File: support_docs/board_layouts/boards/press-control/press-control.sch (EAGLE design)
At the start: 14 parts, among them X3 6ESRM-P, X4 6ESRM-P

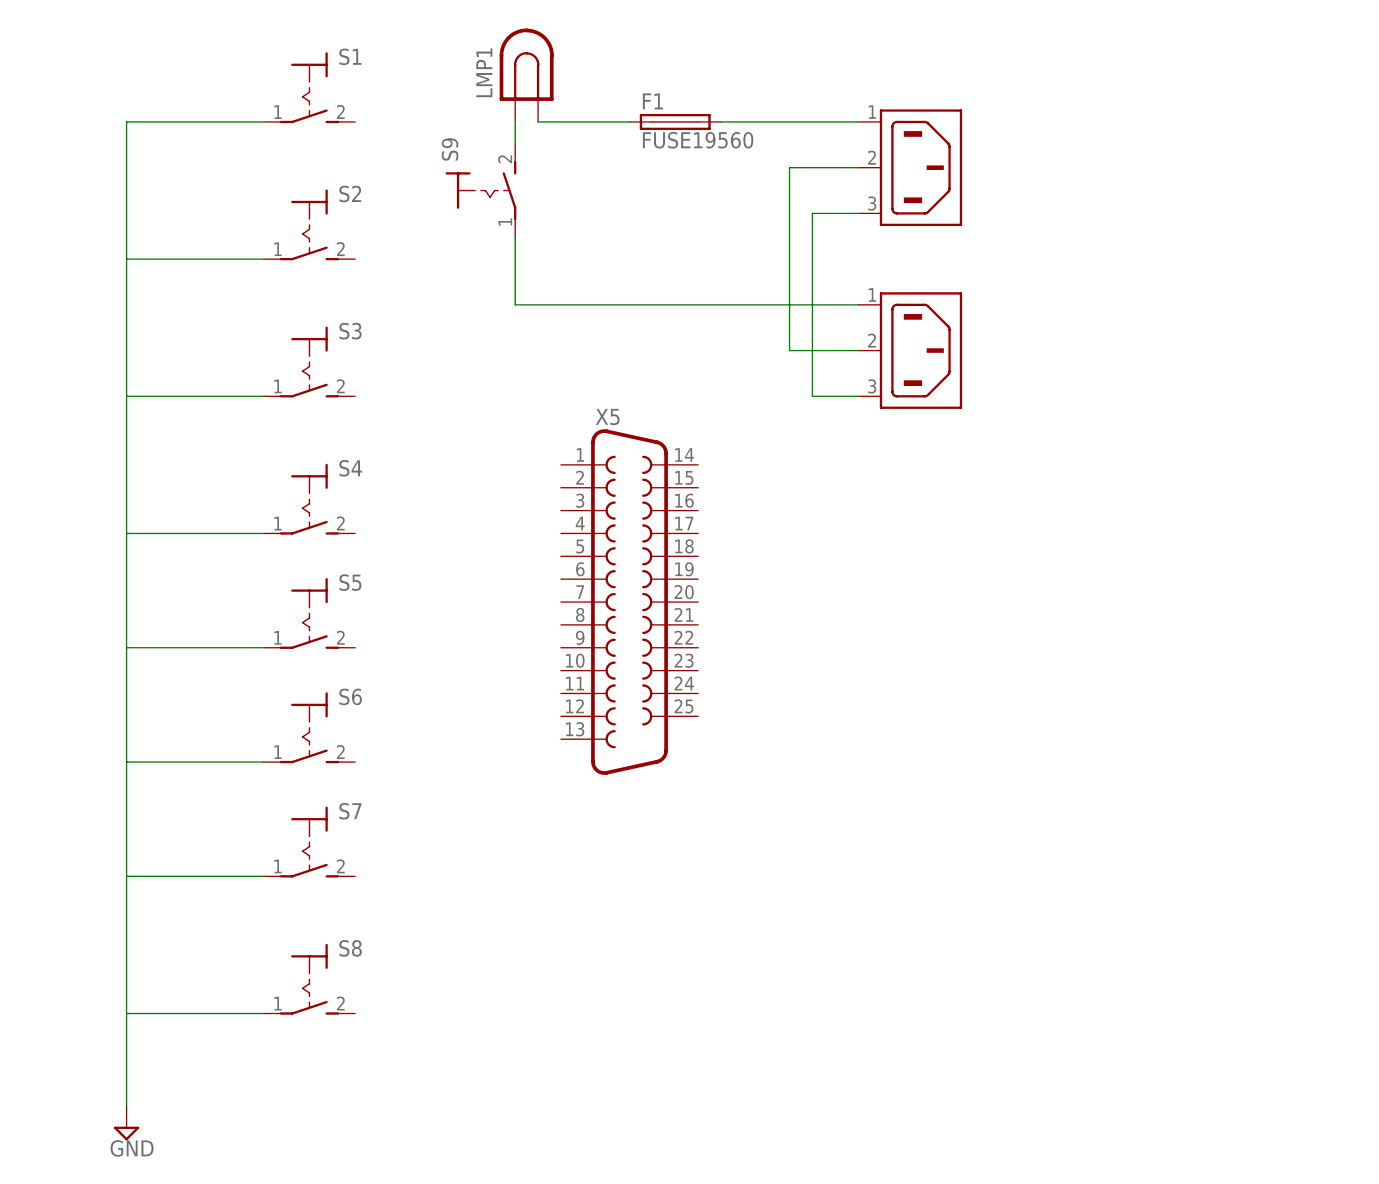
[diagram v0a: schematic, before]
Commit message: redesign - not enough io pins
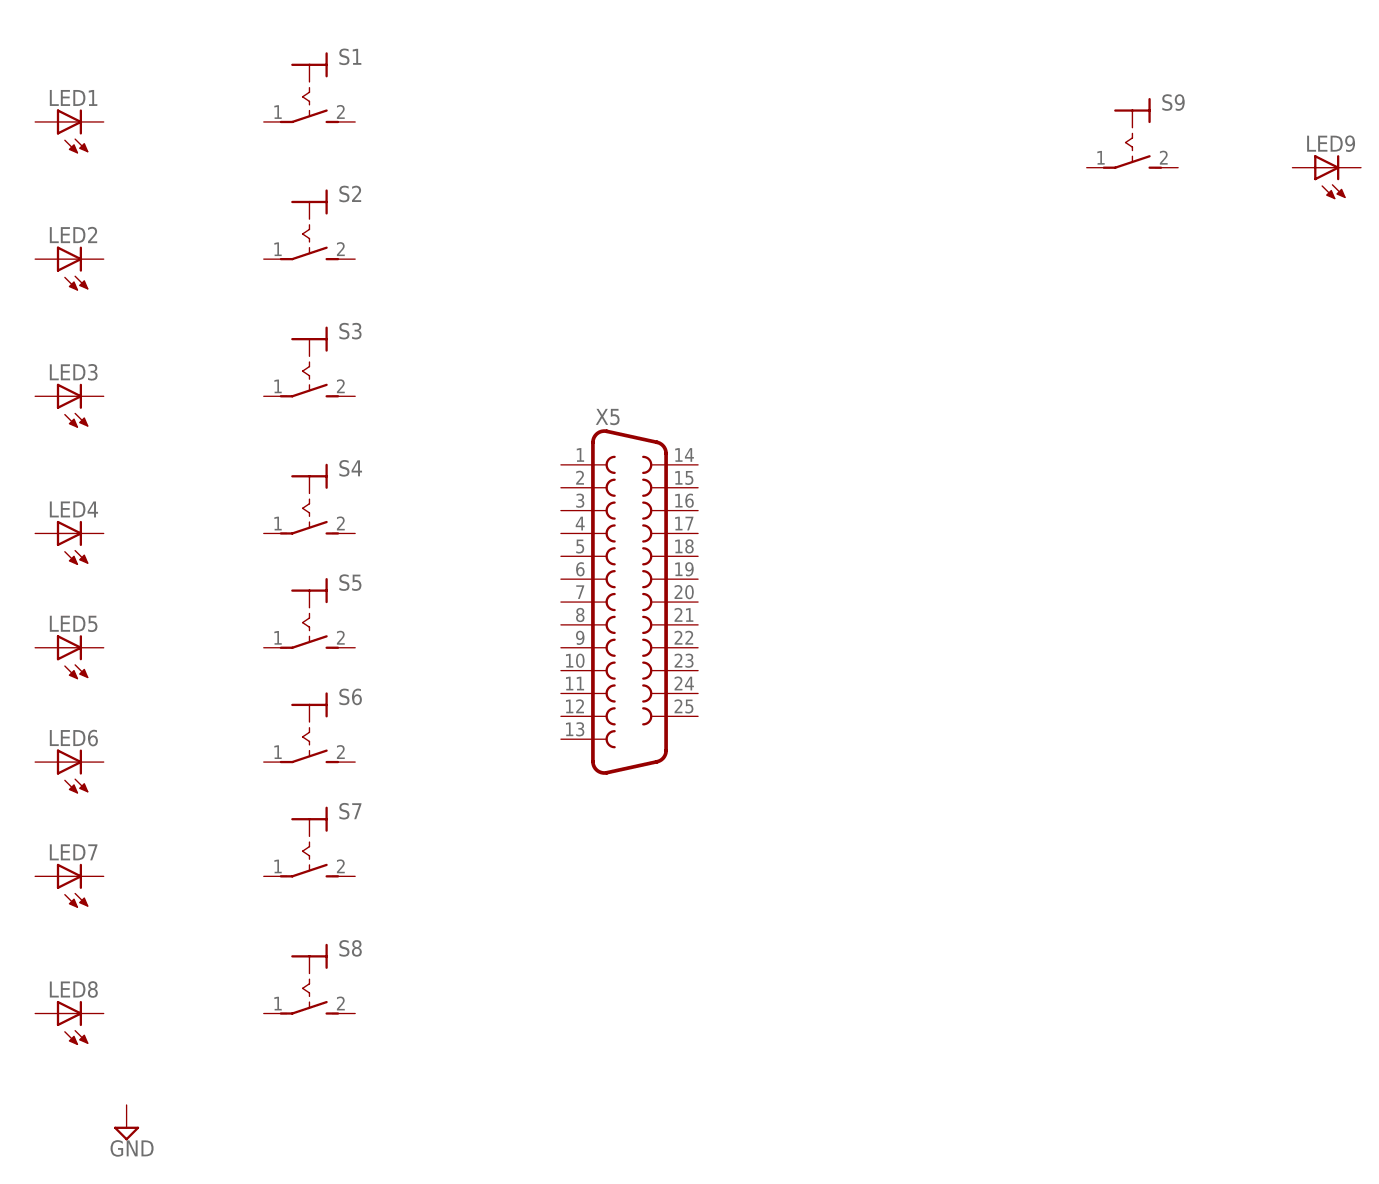
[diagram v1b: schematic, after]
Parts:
- removed F1: FUSE19560, fuse:FUSE19560
- removed LMP1: (no value), special:LAMP
- removed X3, X4: 6ESRM-P, con-tycoelectronics:6ESRM-P
- added LED1, LED2, LED3, LED4, LED5, LED6, LED7, LED8, LED9: (no value), adafruit:LED5MM
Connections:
- removed net GND: S1.P, S2.P, S3.P, S4.P, S5.P, S6.P, S7.P, S8.P
- removed net N$2: F1.2, X3.AC1
- removed net N$3: F1.1, LMP1.2
- removed net N$4: LMP1.1, S9.S
- removed net N$5: S9.P, X4.AC1
- removed net N$6: X3.SH, X4.SH
- removed net N$7: X3.AC2, X4.AC2
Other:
- moved on the sheet: S9
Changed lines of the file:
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@@
 <?xml version="1.0" encoding="utf-8"?>
 <!DOCTYPE eagle SYSTEM "eagle.dtd">
-<eagle version="8.4.2">
+<eagle version="8.4.3">
 <drawing>
 <settings>
@@
 <layer number="230" name="230bmp" color="7" fill="1" visible="yes" active="yes"/>
 <layer number="231" name="231bmp" color="7" fill="1" visible="yes" active="yes"/>
+<layer number="232" name="Eagle3D_PG2" color="7" fill="1" visible="no" active="no"/>
+<layer number="233" name="Eagle3D_PG3" color="7" fill="1" visible="no" active="no"/>
 <layer number="248" name="Housing" color="7" fill="1" visible="no" active="yes"/>
 <layer number="249" name="Edge" color="7" fill="1" visible="no" active="yes"/>
@@
 <part name="S8" library="switch" library_urn="urn:adsk.eagle:library:380" deviceset="MS243" device="" package3d_urn="urn:adsk.eagle:package:27683/1"/>
 <part name="SUPPLY1" library="supply2" library_urn="urn:adsk.eagle:library:372" deviceset="GND" device=""/>
-<part name="F1" library="fuse" library_urn="urn:adsk.eagle:library:233" deviceset="FUSE" device="19560" package3d_urn="urn:adsk.eagle:package:14057/1"/>
-<part name="X3" library="con-tycoelectronics" library_urn="urn:adsk.eagle:library:193" deviceset="6ESRM-P" device="" package3d_urn="urn:adsk.eagle:package:10655/1"/>
 <part name="S9" library="switch" library_urn="urn:adsk.eagle:library:380" deviceset="MS243" device="" package3d_urn="urn:adsk.eagle:package:27683/1"/>
-<part name="LMP1" library="special" library_urn="urn:adsk.eagle:library:367" deviceset="LAMP" device="" package3d_urn="urn:adsk.eagle:package:26651/1"/>
-<part name="X4" library="con-tycoelectronics" library_urn="urn:adsk.eagle:library:193" deviceset="6ESRM-P" device="" package3d_urn="urn:adsk.eagle:package:10655/1"/>
 <part name="X5" library="SparkFun-Retired" library_urn="urn:adsk.eagle:library:533" deviceset="DB25_FEMALE" device="V"/>
+<part name="LED1" library="adafruit" library_urn="urn:adsk.eagle:library:420" deviceset="LED" device="5MM"/>
+<part name="LED2" library="adafruit" library_urn="urn:adsk.eagle:library:420" deviceset="LED" device="5MM"/>
+<part name="LED3" library="adafruit" library_urn="urn:adsk.eagle:library:420" deviceset="LED" device="5MM"/>
+<part name="LED4" library="adafruit" library_urn="urn:adsk.eagle:library:420" deviceset="LED" device="5MM"/>
+<part name="LED5" library="adafruit" library_urn="urn:adsk.eagle:library:420" deviceset="LED" device="5MM"/>
+<part name="LED6" library="adafruit" library_urn="urn:adsk.eagle:library:420" deviceset="LED" device="5MM"/>
+<part name="LED7" library="adafruit" library_urn="urn:adsk.eagle:library:420" deviceset="LED" device="5MM"/>
+<part name="LED8" library="adafruit" library_urn="urn:adsk.eagle:library:420" deviceset="LED" device="5MM"/>
+<part name="LED9" library="adafruit" library_urn="urn:adsk.eagle:library:420" deviceset="LED" device="5MM"/>
 </parts>
 <sheets>
@@
 <instance part="S8" gate="1" x="-2.54" y="10.16" rot="R270"/>
 <instance part="SUPPLY1" gate="GND" x="-22.86" y="-5.08"/>
-<instance part="F1" gate="G$1" x="38.1" y="106.68"/>
-<instance part="X3" gate="G$1" x="60.96" y="101.6"/>
-<instance part="S9" gate="1" x="17.78" y="99.06"/>
-<instance part="LMP1" gate="G$1" x="20.32" y="111.76"/>
-<instance part="X4" gate="G$1" x="60.96" y="81.28"/>
+<instance part="S9" gate="1" x="88.9" y="104.14" rot="R270"/>
 <instance part="X5" gate="-1" x="33.02" y="53.34"/>
+<instance part="LED1" gate="G$1" x="-30.48" y="106.68" rot="R90"/>
+<instance part="LED2" gate="G$1" x="-30.48" y="91.44" rot="R90"/>
+<instance part="LED3" gate="G$1" x="-30.48" y="76.2" rot="R90"/>
+<instance part="LED4" gate="G$1" x="-30.48" y="60.96" rot="R90"/>
+<instance part="LED5" gate="G$1" x="-30.48" y="48.26" rot="R90"/>
+<instance part="LED6" gate="G$1" x="-30.48" y="35.56" rot="R90"/>
+<instance part="LED7" gate="G$1" x="-30.48" y="22.86" rot="R90"/>
+<instance part="LED8" gate="G$1" x="-30.48" y="7.62" rot="R90"/>
+<instance part="LED9" gate="G$1" x="109.22" y="101.6" rot="R90"/>
 </instances>
 <busses>
 </busses>
 <nets>
-<net name="GND" class="0">
-<segment>
-<pinref part="S1" gate="1" pin="P"/>
-<wire x1="-7.62" y1="106.68" x2="-22.86" y2="106.68" width="0.1524" layer="91"/>
-<wire x1="-22.86" y1="106.68" x2="-22.86" y2="91.44" width="0.1524" layer="91"/>
-<pinref part="S2" gate="1" pin="P"/>
-<wire x1="-7.62" y1="91.44" x2="-22.86" y2="91.44" width="0.1524" layer="91"/>
-<pinref part="S3" gate="1" pin="P"/>
-<wire x1="-22.86" y1="91.44" x2="-22.86" y2="76.2" width="0.1524" layer="91"/>
-<wire x1="-7.62" y1="76.2" x2="-22.86" y2="76.2" width="0.1524" layer="91"/>
-<pinref part="S4" gate="1" pin="P"/>
-<wire x1="-22.86" y1="76.2" x2="-22.86" y2="60.96" width="0.1524" layer="91"/>
-<wire x1="-7.62" y1="60.96" x2="-22.86" y2="60.96" width="0.1524" layer="91"/>
-<pinref part="S5" gate="1" pin="P"/>
-<wire x1="-22.86" y1="60.96" x2="-22.86" y2="48.26" width="0.1524" layer="91"/>
-<wire x1="-7.62" y1="48.26" x2="-22.86" y2="48.26" width="0.1524" layer="91"/>
-<pinref part="S6" gate="1" pin="P"/>
-<wire x1="-22.86" y1="48.26" x2="-22.86" y2="35.56" width="0.1524" layer="91"/>
-<wire x1="-7.62" y1="35.56" x2="-22.86" y2="35.56" width="0.1524" layer="91"/>
-<wire x1="-22.86" y1="35.56" x2="-22.86" y2="22.86" width="0.1524" layer="91"/>
-<pinref part="S7" gate="1" pin="P"/>
-<wire x1="-7.62" y1="22.86" x2="-22.86" y2="22.86" width="0.1524" layer="91"/>
-<wire x1="-22.86" y1="22.86" x2="-22.86" y2="7.62" width="0.1524" layer="91"/>
-<pinref part="S8" gate="1" pin="P"/>
-<wire x1="-22.86" y1="7.62" x2="-7.62" y2="7.62" width="0.1524" layer="91"/>
-<pinref part="SUPPLY1" gate="GND" pin="GND"/>
-<wire x1="-22.86" y1="7.62" x2="-22.86" y2="-2.54" width="0.1524" layer="91"/>
-</segment>
-</net>
-<net name="N$2" class="0">
-<segment>
-<pinref part="X3" gate="G$1" pin="AC1"/>
-<pinref part="F1" gate="G$1" pin="2"/>
-<wire x1="58.42" y1="106.68" x2="43.18" y2="106.68" width="0.1524" layer="91"/>
-</segment>
-</net>
-<net name="N$3" class="0">
-<segment>
-<pinref part="F1" gate="G$1" pin="1"/>
-<pinref part="LMP1" gate="G$1" pin="2"/>
-<wire x1="33.02" y1="106.68" x2="22.86" y2="106.68" width="0.1524" layer="91"/>
-</segment>
-</net>
-<net name="N$4" class="0">
-<segment>
-<pinref part="S9" gate="1" pin="S"/>
-<pinref part="LMP1" gate="G$1" pin="1"/>
-<wire x1="20.32" y1="104.14" x2="20.32" y2="106.68" width="0.1524" layer="91"/>
-</segment>
-</net>
-<net name="N$5" class="0">
-<segment>
-<pinref part="S9" gate="1" pin="P"/>
-<wire x1="20.32" y1="93.98" x2="20.32" y2="86.36" width="0.1524" layer="91"/>
-<pinref part="X4" gate="G$1" pin="AC1"/>
-<wire x1="20.32" y1="86.36" x2="58.42" y2="86.36" width="0.1524" layer="91"/>
-</segment>
-</net>
-<net name="N$6" class="0">
-<segment>
-<pinref part="X3" gate="G$1" pin="SH"/>
-<wire x1="58.42" y1="101.6" x2="50.8" y2="101.6" width="0.1524" layer="91"/>
-<wire x1="50.8" y1="101.6" x2="50.8" y2="81.28" width="0.1524" layer="91"/>
-<pinref part="X4" gate="G$1" pin="SH"/>
-<wire x1="50.8" y1="81.28" x2="58.42" y2="81.28" width="0.1524" layer="91"/>
-</segment>
-</net>
-<net name="N$7" class="0">
-<segment>
-<pinref part="X3" gate="G$1" pin="AC2"/>
-<wire x1="58.42" y1="96.52" x2="53.34" y2="96.52" width="0.1524" layer="91"/>
-<pinref part="X4" gate="G$1" pin="AC2"/>
-<wire x1="53.34" y1="96.52" x2="53.34" y2="76.2" width="0.1524" layer="91"/>
-<wire x1="53.34" y1="76.2" x2="58.42" y2="76.2" width="0.1524" layer="91"/>
-</segment>
-</net>
 </nets>
 </sheet>

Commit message: new board design
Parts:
- added R1, R2, R3, R4, R5, R6, R7, R8, R9: (no value), resistor:R-US_0207/10
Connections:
- new net GND: R1.1, R2.1, R3.1, R4.1, R5.1, R6.1, R7.1, R8.1, R9.1, S1.S, S2.S, S3.S, S4.S, S5.S, S6.S, S7.S, S8.S, X5.10, X5.22
- new net N$1: LED1.C, R1.2
- new net N$10: LED5.A, X5.5
- new net N$11: LED3.A, X5.3
- new net N$12: LED2.A, X5.2
- new net N$13: LED1.A, X5.1
- new net N$14: LED6.A, X5.6
- new net N$15: LED7.A, X5.7
- new net N$16: LED8.A, X5.8
- new net N$17: S5.P, X5.18
- new net N$18: S4.P, X5.17
- new net N$19: S3.P, X5.16
- new net N$2: LED2.C, R2.2
- new net N$20: S2.P, X5.15
- new net N$21: S1.P, X5.14
- new net N$22: S6.P, X5.19
- new net N$23: S7.P, X5.20
- new net N$24: S8.P, X5.21
- new net N$25: S9.S, X5.13
- new net N$26: S9.P, X5.25
- new net N$27: LED9.A, X5.9
- new net N$28: LED9.C, R9.2
- new net N$3: LED3.C, R3.2
- new net N$4: LED4.C, R4.2
- new net N$5: LED5.C, R5.2
- new net N$6: LED6.C, R6.2
- new net N$7: LED7.C, R7.2
- new net N$8: LED8.C, R8.2
- new net N$9: LED4.A, X5.4
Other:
- moved on the sheet: LED1, LED2, LED3, LED4, LED5, LED6, LED7, LED8, LED9, S1, S2, S3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
